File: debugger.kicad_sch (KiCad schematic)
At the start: 15 parts, among them J2 MCU_SWD, J3 TC_SWD, U2 ATSAMD11

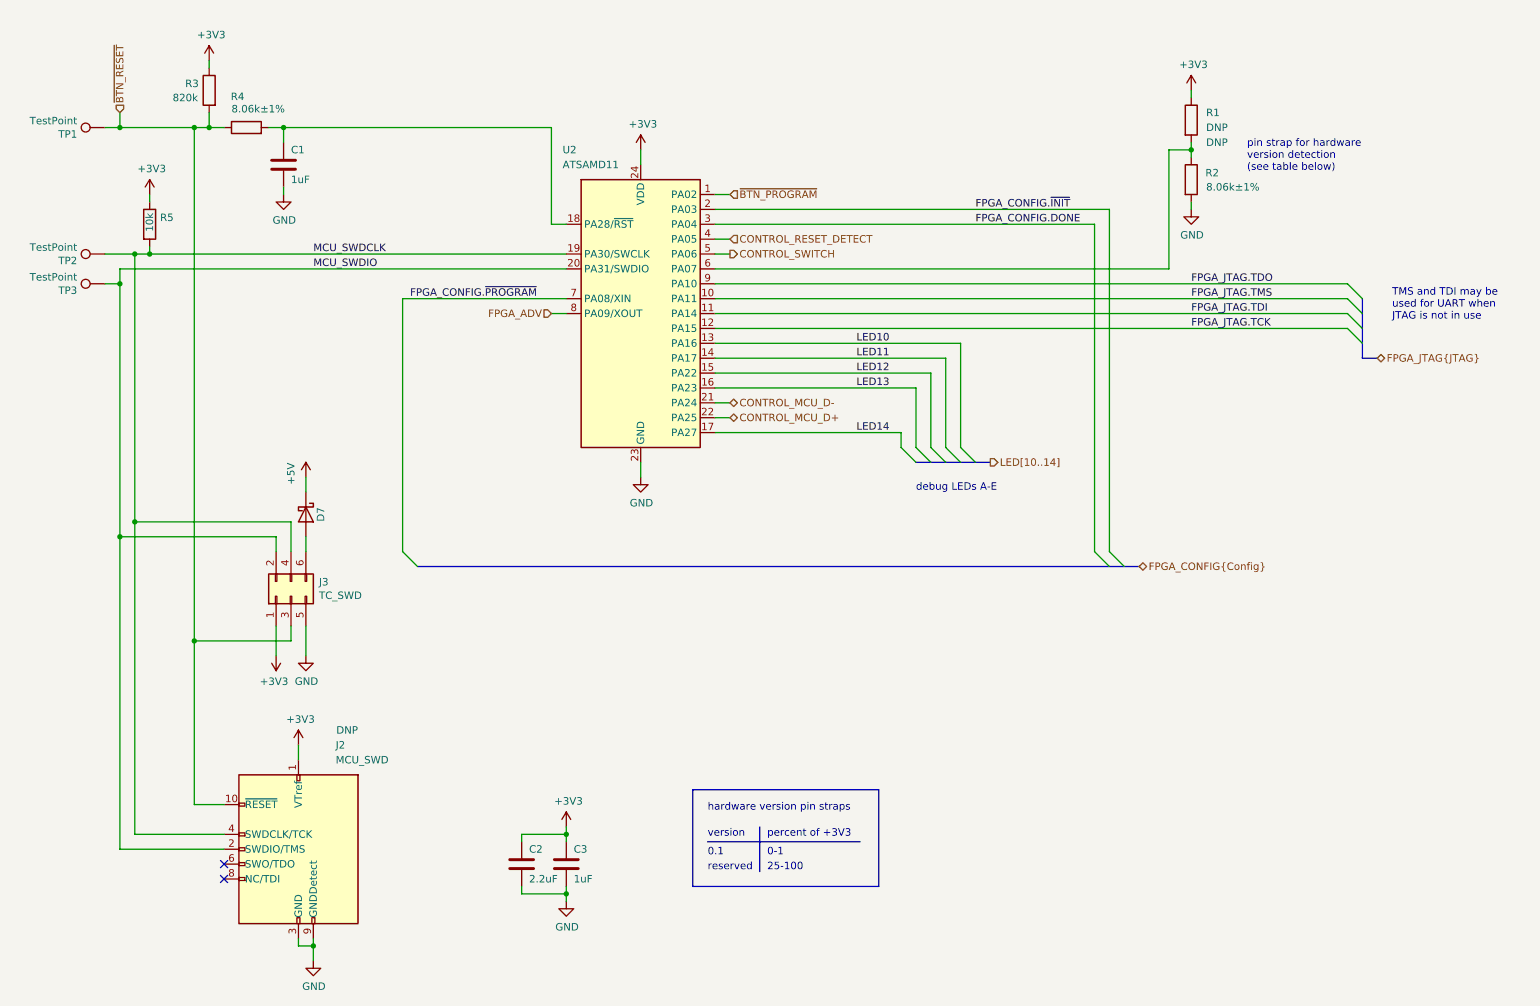
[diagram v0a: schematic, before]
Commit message: Add radio transceiver
Remove Cynthion-specific features
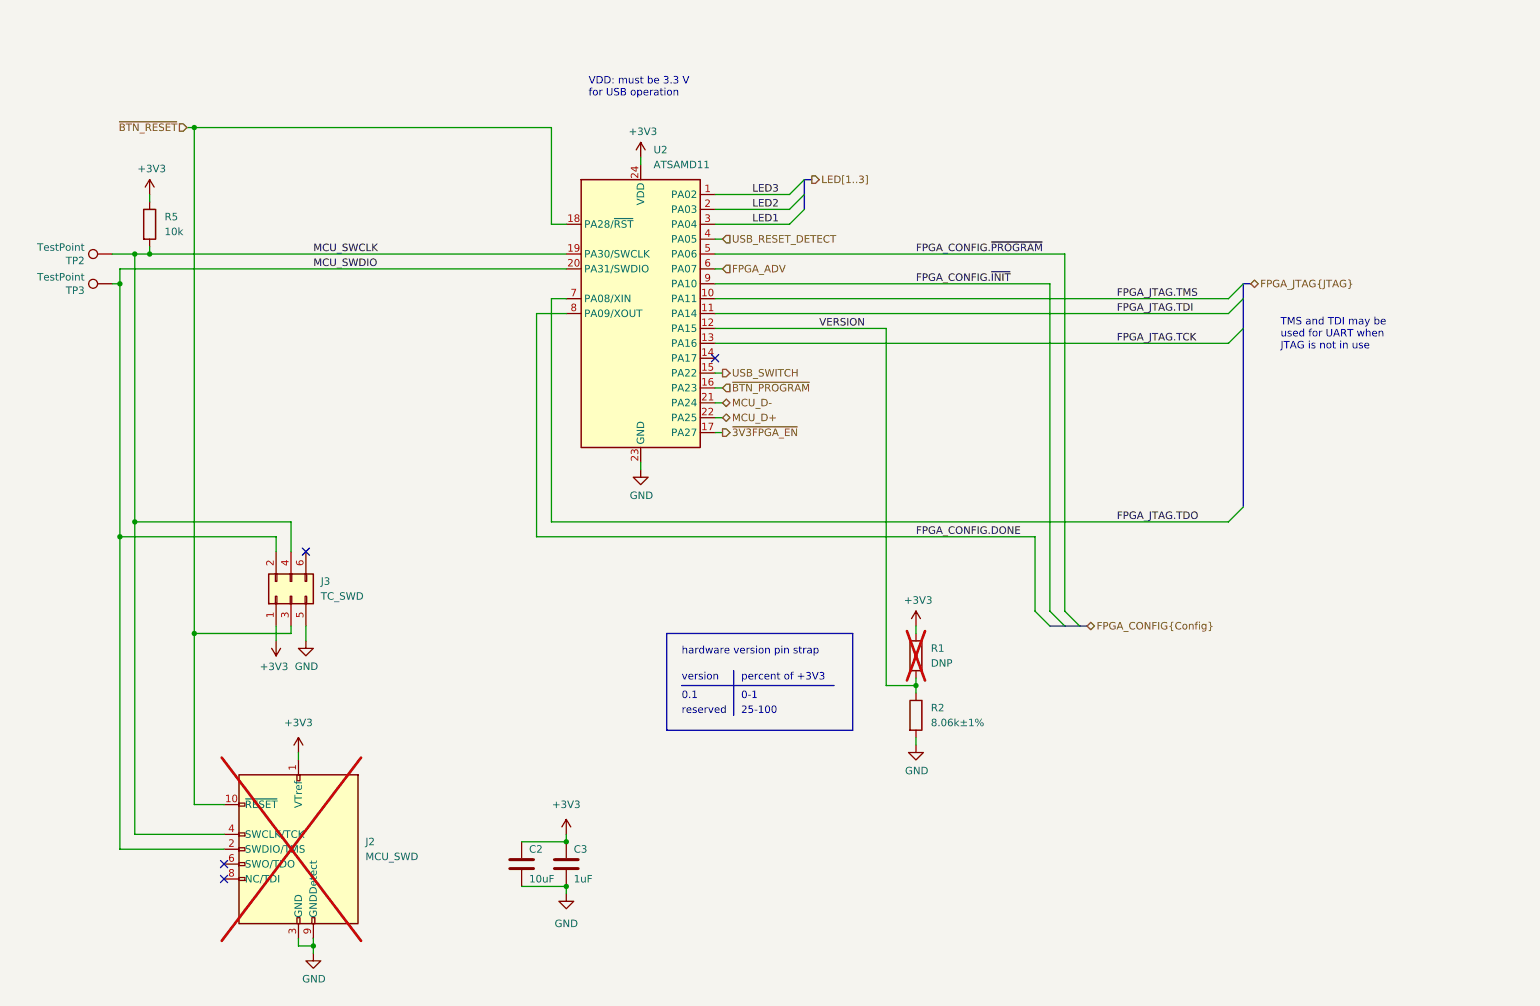
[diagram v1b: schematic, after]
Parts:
- removed C1: 1uF, Capacitor_SMD:C_0402_1005Metric, symbol Device:C
- removed D7: SCHOTTKY, mainboard:DSN1006-2, symbol Device:D_Schottky
- removed R3: 820k, Resistor_SMD:R_0402_1005Metric, symbol Device:R
- removed R4: 8.06k±1%, Resistor_SMD:R_0402_1005Metric, symbol Device:R
- removed TP1: TestPoint, TestPoint:TestPoint_Pad_D1.0mm, symbol Connector:TestPoint
- C2: value 2.2uF -> 10uF; Part Number CL10A225KP8NNNC -> CL10A106KP8NNNC
- C3: Part Number CL05A105MQ5NNNC -> CL05A105KP5NNNC; Substitution CL05A105KQ5NNNC, CL05A105KP5NNNC, CL05A105KO5NNNC -> any equivalent
- J2: DNP DNP -> (none); now not fitted
- R1: DNP DNP -> (none); Manufacturer Yageo -> (none); Substitution any equivalent -> (none); now not fitted
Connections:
- net CONTROL_SWITCH is gone; now on net FPGA_CONFIG.~{PROGRAM}: U2.5 (PA06)
- net LED10 is gone; now on net FPGA_JTAG.TCK: U2.13 (PA16)
- net LED13 is gone; now on net ~{BTN_PROGRAM}: U2.16 (PA23)
- net FPGA_ADV: now also U2.6 (PA07); no longer U2.8 (PA09/XOUT)
- net FPGA_CONFIG.DONE: now also U2.8 (PA09/XOUT); no longer U2.3 (PA04)
- net FPGA_CONFIG.~{INIT}: now also U2.9 (PA10); no longer U2.2 (PA03)
- net FPGA_CONFIG.~{PROGRAM}: no longer U2.7 (PA08/XIN)
- net FPGA_JTAG.TCK: no longer U2.12 (PA15)
- net FPGA_JTAG.TDO: now also U2.7 (PA08/XIN); no longer U2.9 (PA10)
- net ~{BTN_PROGRAM}: no longer U2.1 (PA02)
- net ~{BTN_RESET}: now also U2.18 (PA28/~{RST})
- net VERSION: now reaches R1.2, R2.1
- net VERSION: now also U2.12 (PA15); no longer U2.6 (PA07)
- net CONTROL_MCU_D+ renamed MCU_D+
- net CONTROL_MCU_D- renamed MCU_D-
- net CONTROL_RESET_DETECT renamed USB_RESET_DETECT
- net LED11: no longer names the net of U2.14 (PA17)
- net LED12 renamed USB_SWITCH
- net LED14 renamed ~{3V3FPGA_EN}
- net MCU_SWDCLK renamed MCU_SWCLK
- new net LED1: U2.3 (PA04)
- new net LED2: U2.2 (PA03)
- new net LED3: U2.1 (PA02)
- no-connect marks 2 -> 4
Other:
- note added: "VDD: must be 3.3 V for USB operation"
- note added: "hardware version pin strap"
- note removed: "debug LEDs A-E"
- note removed: "hardware version pin straps"
- note removed: "pin strap for hardware version detection (see table below)"
- company: Copyright 2023 Great Scott Gadgets -> ${COPYRIGHT}
- title: URTI Mainboard -> ${TITLE}
- moved on the sheet: R2, TP2, TP3

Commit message: Update mcu pin assignments to support fast JTAG
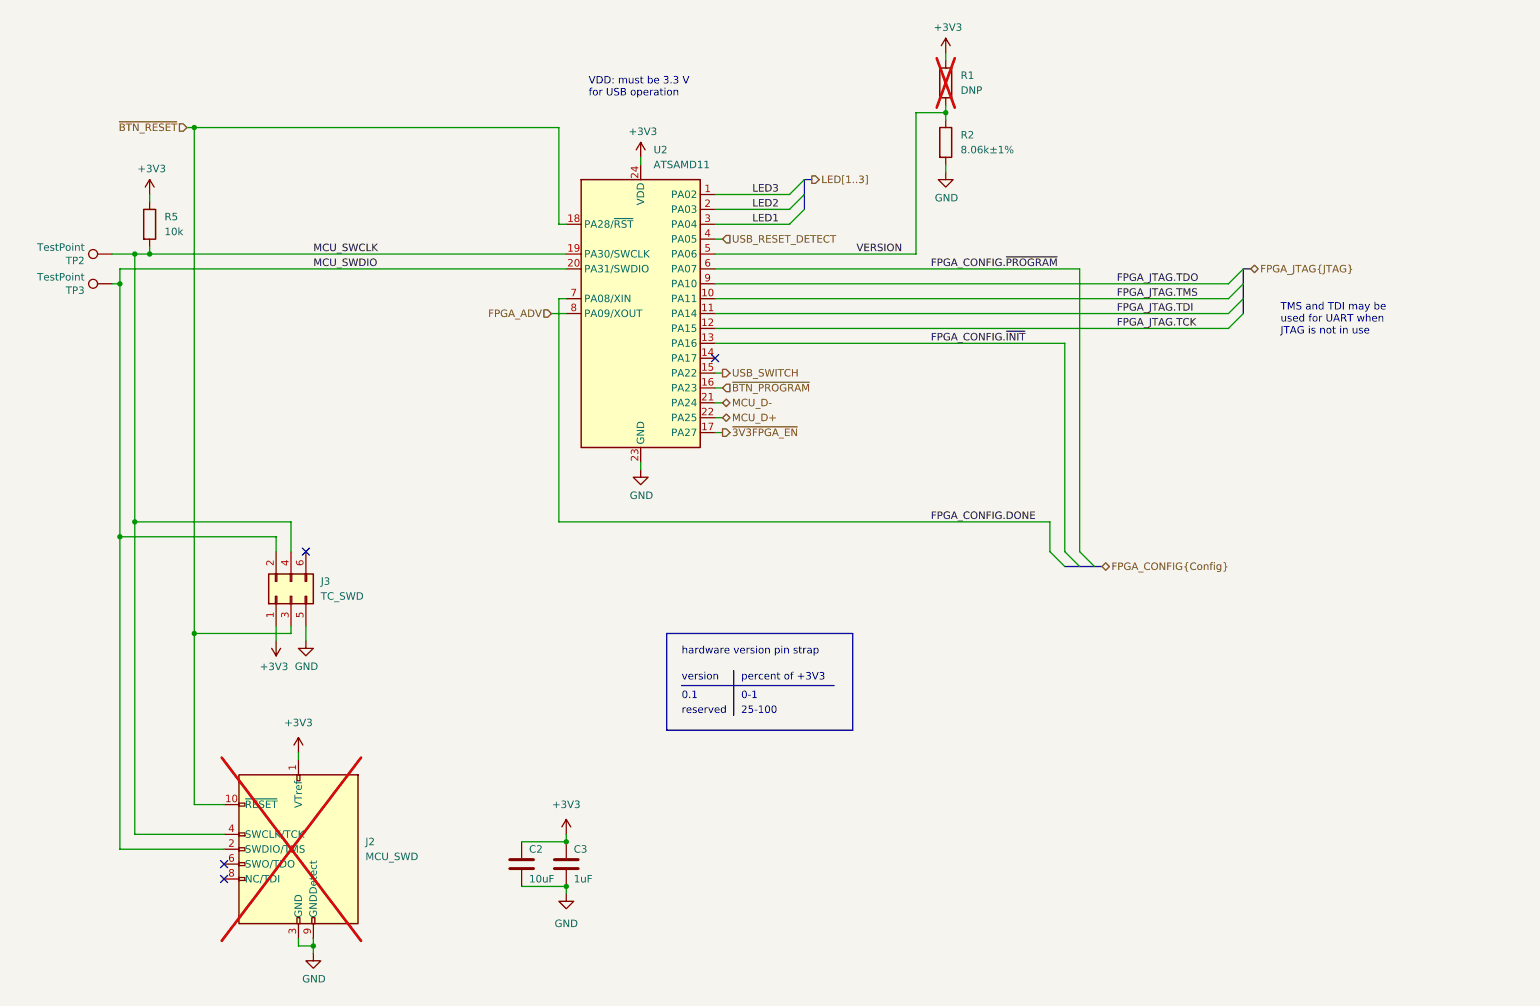
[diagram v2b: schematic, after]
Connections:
- net FPGA_ADV: now also U2.8 (PA09/XOUT); no longer U2.6 (PA07)
- net FPGA_CONFIG.DONE: now also U2.7 (PA08/XIN); no longer U2.8 (PA09/XOUT)
- net FPGA_CONFIG.~{INIT}: now also U2.13 (PA16); no longer U2.9 (PA10)
- net FPGA_CONFIG.~{PROGRAM}: now also U2.6 (PA07); no longer U2.5 (PA06)
- net FPGA_JTAG.TCK: now also U2.12 (PA15); no longer U2.13 (PA16)
- net FPGA_JTAG.TDO: now also U2.9 (PA10); no longer U2.7 (PA08/XIN)
- net VERSION: now also U2.5 (PA06); no longer U2.12 (PA15)
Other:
- moved on the sheet: R1, R2
